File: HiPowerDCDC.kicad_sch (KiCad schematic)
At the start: 57 parts, among them J1 Conn_01x01, J2 Conn_01x01, J3 Conn_01x01, J4 Conn_01x01, J5 Conn_01x04, Q1 WMJ38N60, Q2 WMJ38N60, SW1 SW_Push, SW2 SW_Push, U1 ESP32-WROOM-32U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

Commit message: Changed to high voltage capacitors
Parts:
- C11, C12, C13, C14: footprint Capacitor_SMD:C_1206_3216Metric -> Capacitor_SMD:C_1812_4532Metric
- R10: footprint Resistor_SMD:R_1206_3216Metric -> Resistor_SMD:R_1812_4532Metric
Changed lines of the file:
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@@
       (effects (font (size 1.27 1.27)) (justify left))
     )
-    (property "Footprint" "Resistor_SMD:R_1206_3216Metric" (id 2) (at 184.277 137.795 90)
+    (property "Footprint" "Resistor_SMD:R_1812_4532Metric" (id 2) (at 184.277 137.795 90)
       (effects (font (size 1.27 1.27)) hide)
     )
@@
       (effects (font (size 1.27 1.27)) (justify left))
     )
-    (property "Footprint" "Capacitor_SMD:C_1206_3216Metric" (id 2) (at 204.1652 83.185 0)
+    (property "Footprint" "Capacitor_SMD:C_1812_4532Metric" (id 2) (at 204.1652 83.185 0)
       (effects (font (size 1.27 1.27)) hide)
     )
@@
       (effects (font (size 1.27 1.27)) (justify left))
     )
-    (property "Footprint" "Capacitor_SMD:C_1206_3216Metric" (id 2) (at 204.1652 139.7 0)
+    (property "Footprint" "Capacitor_SMD:C_1812_4532Metric" (id 2) (at 204.1652 139.7 0)
       (effects (font (size 1.27 1.27)) hide)
     )
@@
       (effects (font (size 1.27 1.27)) (justify left))
     )
-    (property "Footprint" "Capacitor_SMD:C_1206_3216Metric" (id 2) (at 209.8802 83.185 0)
+    (property "Footprint" "Capacitor_SMD:C_1812_4532Metric" (id 2) (at 209.8802 83.185 0)
       (effects (font (size 1.27 1.27)) hide)
     )
@@
       (effects (font (size 1.27 1.27)) (justify left))
     )
-    (property "Footprint" "Capacitor_SMD:C_1206_3216Metric" (id 2) (at 209.8802 139.7 0)
+    (property "Footprint" "Capacitor_SMD:C_1812_4532Metric" (id 2) (at 209.8802 139.7 0)
       (effects (font (size 1.27 1.27)) hide)
     )
@@
     )
     (path "/1d6ca196-d190-42cc-82e2-dd05479e359d"
-      (reference "C11") (unit 1) (value "10n") (footprint "Capacitor_SMD:C_1206_3216Metric")
+      (reference "C11") (unit 1) (value "10n") (footprint "Capacitor_SMD:C_1812_4532Metric")
     )
     (path "/40521bdb-9910-4911-97bc-1c460c9e71b9"
-      (reference "C12") (unit 1) (value "10n") (footprint "Capacitor_SMD:C_1206_3216Metric")
+      (reference "C12") (unit 1) (value "10n") (footprint "Capacitor_SMD:C_1812_4532Metric")
     )
     (path "/116f1552-f56f-4cf6-88c9-0aac35b221be"
-      (reference "C13") (unit 1) (value "10n") (footprint "Capacitor_SMD:C_1206_3216Metric")
+      (reference "C13") (unit 1) (value "10n") (footprint "Capacitor_SMD:C_1812_4532Metric")
     )
     (path "/e4d3f805-887c-499c-a2d1-0322c8808f2b"
-      (reference "C14") (unit 1) (value "10n") (footprint "Capacitor_SMD:C_1206_3216Metric")
+      (reference "C14") (unit 1) (value "10n") (footprint "Capacitor_SMD:C_1812_4532Metric")
     )
     (path "/212825e7-4ffe-4953-87c8-beb79db8e49b"
@@
     )
     (path "/f27ca728-3ec4-4b64-b597-7f763991f368"
-      (reference "R10") (unit 1) (value "10M") (footprint "Resistor_SMD:R_1206_3216Metric")
+      (reference "R10") (unit 1) (value "10M") (footprint "Resistor_SMD:R_1812_4532Metric")
     )
     (path "/31561b39-b331-494c-9b8f-ce3ac83f19cc"

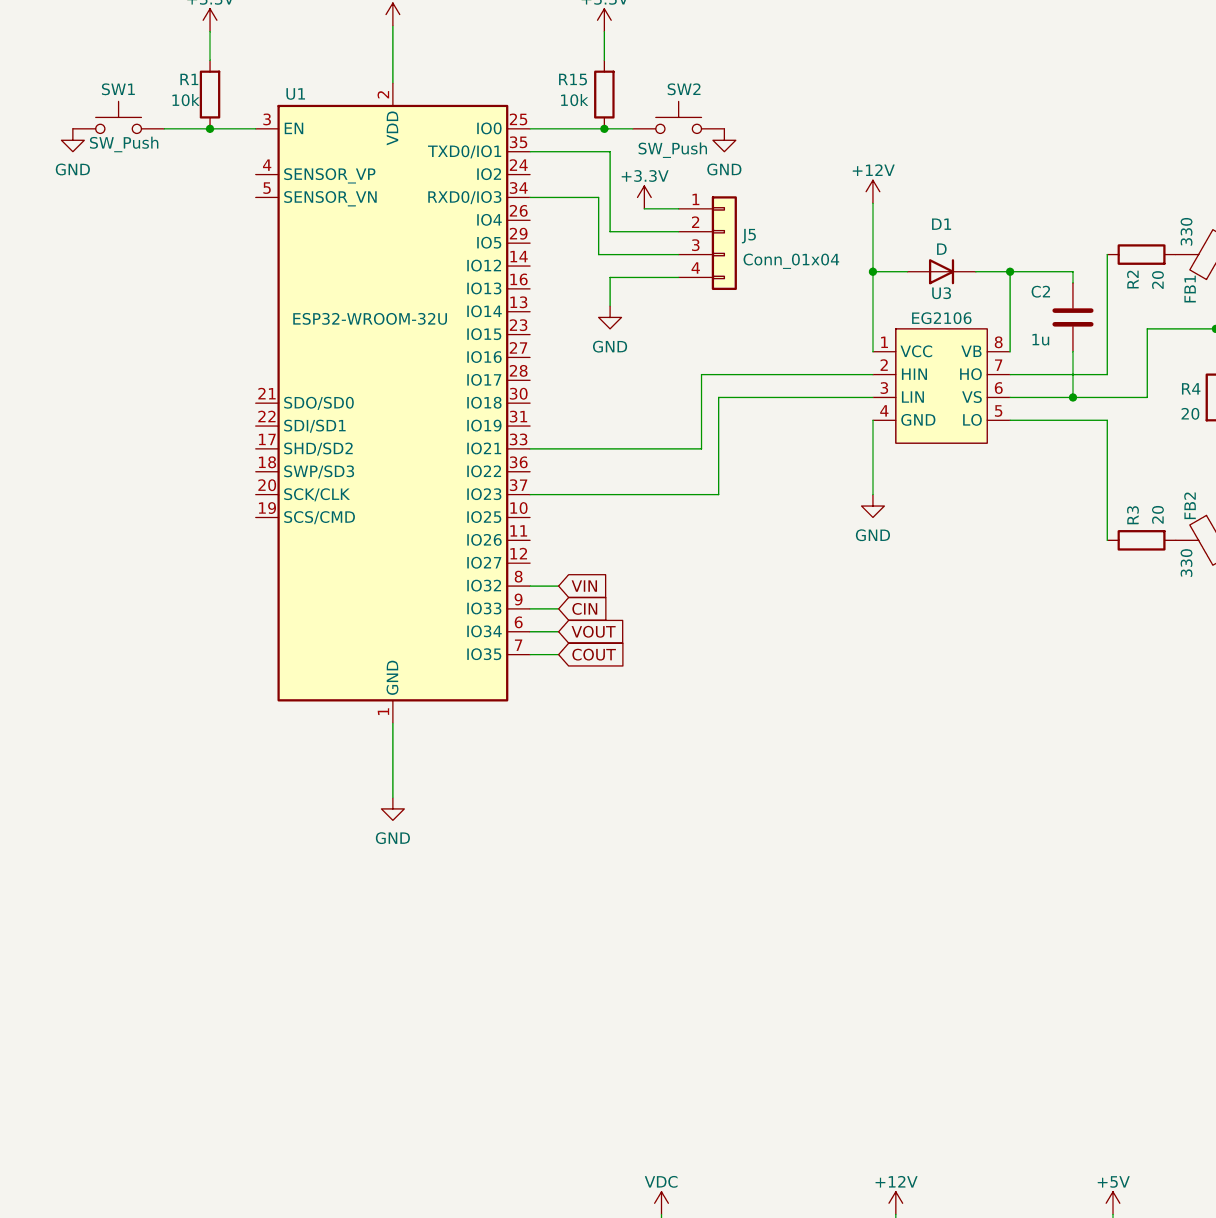
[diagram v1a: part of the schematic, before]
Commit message: Added PTC sensor, Laci you didn't check me :(
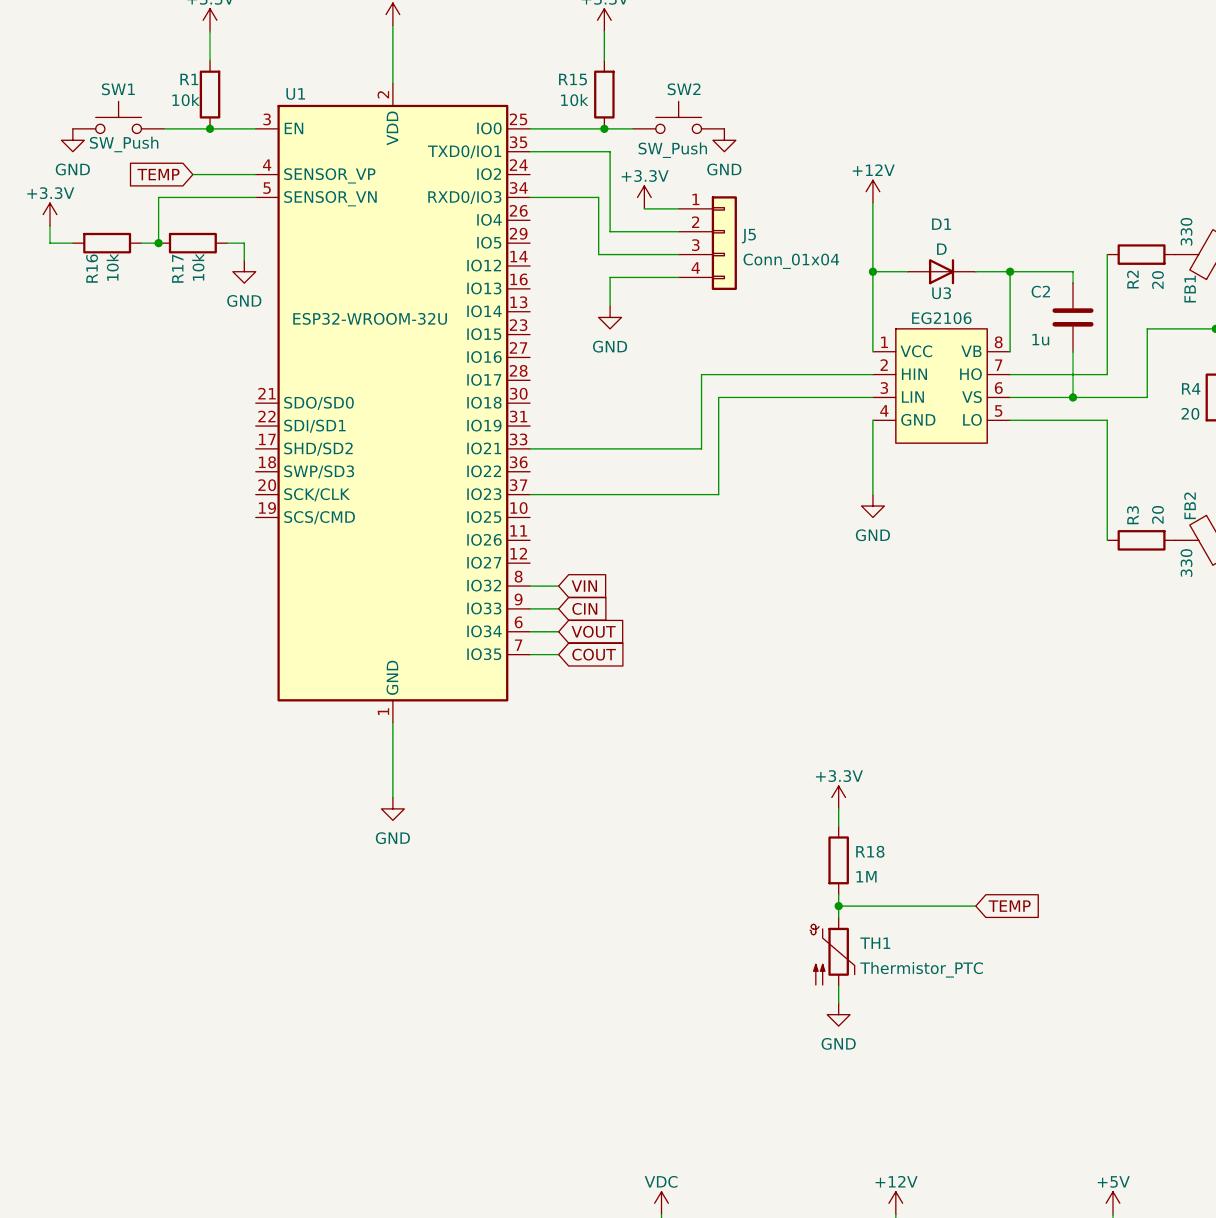
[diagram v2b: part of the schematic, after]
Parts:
- added R16, R17: 10k, Resistor_SMD:R_1206_3216Metric, symbol Device:R
- added R18: 1M, Resistor_SMD:R_1206_3216Metric, symbol Device:R
- added TH1: Thermistor_PTC, Connector_PinHeader_2.54mm:PinHeader_1x02_P2.54mm_Vertical, symbol Device:Thermistor_PTC
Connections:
- net +3V3: now also R16.2, R18.1
- net GND: now also R17.1, TH1.2
- net TEMP: now reaches U1.4 (SENSOR_VP)
- net TEMP: now also R18.2, TH1.1
- net at U1.5 (SENSOR_VN): now also R16.1, R17.2

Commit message: Added Keystone connectors
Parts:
- J1, J2, J3, J4: footprint HiPowerFP:Screw_PCB_pin -> HiPowerFP:Keystone_7808
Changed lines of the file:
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@@
       (effects (font (size 1.27 1.27)) (justify left))
     )
-    (property "Footprint" "HiPowerFP:Screw_PCB_pin" (id 2) (at 250.19 75.565 0)
-      (effects (font (size 1.27 1.27)) hide)
-    )
-    (property "Datasheet" "~" (id 3) (at 250.19 75.565 0)
+    (property "Footprint" "HiPowerFP:Keystone_7808" (id 2) (at 250.19 75.565 0)
+      (effects (font (size 1.27 1.27)) hide)
+    )
+    (property "Datasheet" "${KIPRJMOD}/datasheets/7808_keystone.pdf" (id 3) (at 250.19 75.565 0)
       (effects (font (size 1.27 1.27)) hide)
     )
@@
       (effects (font (size 1.27 1.27)) (justify left))
     )
-    (property "Footprint" "HiPowerFP:Screw_PCB_pin" (id 2) (at 250.19 84.455 0)
-      (effects (font (size 1.27 1.27)) hide)
-    )
-    (property "Datasheet" "~" (id 3) (at 250.19 84.455 0)
+    (property "Footprint" "HiPowerFP:Keystone_7808" (id 2) (at 250.19 84.455 0)
+      (effects (font (size 1.27 1.27)) hide)
+    )
+    (property "Datasheet" "${KIPRJMOD}/datasheets/7808_keystone.pdf" (id 3) (at 250.19 84.455 0)
       (effects (font (size 1.27 1.27)) hide)
     )
@@
       (effects (font (size 1.27 1.27)) (justify left))
     )
-    (property "Footprint" "HiPowerFP:Screw_PCB_pin" (id 2) (at 250.19 132.08 0)
-      (effects (font (size 1.27 1.27)) hide)
-    )
-    (property "Datasheet" "~" (id 3) (at 250.19 132.08 0)
+    (property "Footprint" "HiPowerFP:Keystone_7808" (id 2) (at 250.19 132.08 0)
+      (effects (font (size 1.27 1.27)) hide)
+    )
+    (property "Datasheet" "${KIPRJMOD}/datasheets/7808_keystone.pdf" (id 3) (at 250.19 132.08 0)
       (effects (font (size 1.27 1.27)) hide)
     )
@@
       (effects (font (size 1.27 1.27)) (justify left))
     )
-    (property "Footprint" "HiPowerFP:Screw_PCB_pin" (id 2) (at 250.19 140.97 0)
-      (effects (font (size 1.27 1.27)) hide)
-    )
-    (property "Datasheet" "~" (id 3) (at 250.19 140.97 0)
+    (property "Footprint" "HiPowerFP:Keystone_7808" (id 2) (at 250.19 140.97 0)
+      (effects (font (size 1.27 1.27)) hide)
+    )
+    (property "Datasheet" "${KIPRJMOD}/datasheets/7808_keystone.pdf" (id 3) (at 250.19 140.97 0)
       (effects (font (size 1.27 1.27)) hide)
     )
@@
     )
     (path "/56e6dc88-8c88-4439-9853-8d5650f4e59a"
-      (reference "J1") (unit 1) (value "Conn_01x01") (footprint "HiPowerFP:Screw_PCB_pin")
-    )
-    (path "/b86069d6-ba7b-4fda-bab9-b3b8645a27eb"
-      (reference "J2") (unit 1) (value "Conn_01x01") (footprint "HiPowerFP:Screw_PCB_pin")
-    )
-    (path "/a601ba08-1f80-4e43-833f-dc284503f818"
-      (reference "J3") (unit 1) (value "Conn_01x01") (footprint "HiPowerFP:Screw_PCB_pin")
-    )
-    (path "/9db3a826-765e-4e20-9c06-c40423065459"
-      (reference "J4") (unit 1) (value "Conn_01x01") (footprint "HiPowerFP:Screw_PCB_pin")
+      (reference "J1") (unit 1) (value "Conn_01x01") (footprint "HiPowerFP:Keystone_7808")
+    )
+    (path "/06783550-9719-4bf5-8140-cd255df7e49f"
+      (reference "J2") (unit 1) (value "Conn_01x01") (footprint "HiPowerFP:Keystone_7808")
+    )
+    (path "/67875fcf-d422-48b1-a954-a524082b2bfd"
+      (reference "J3") (unit 1) (value "Conn_01x01") (footprint "HiPowerFP:Keystone_7808")
+    )
+    (path "/b9d475bc-116f-4967-8e26-e7975b071a1b"
+      (reference "J4") (unit 1) (value "Conn_01x01") (footprint "HiPowerFP:Keystone_7808")
     )
     (path "/b7572976-7ea1-460a-b8f3-b2f7dbe7301b"

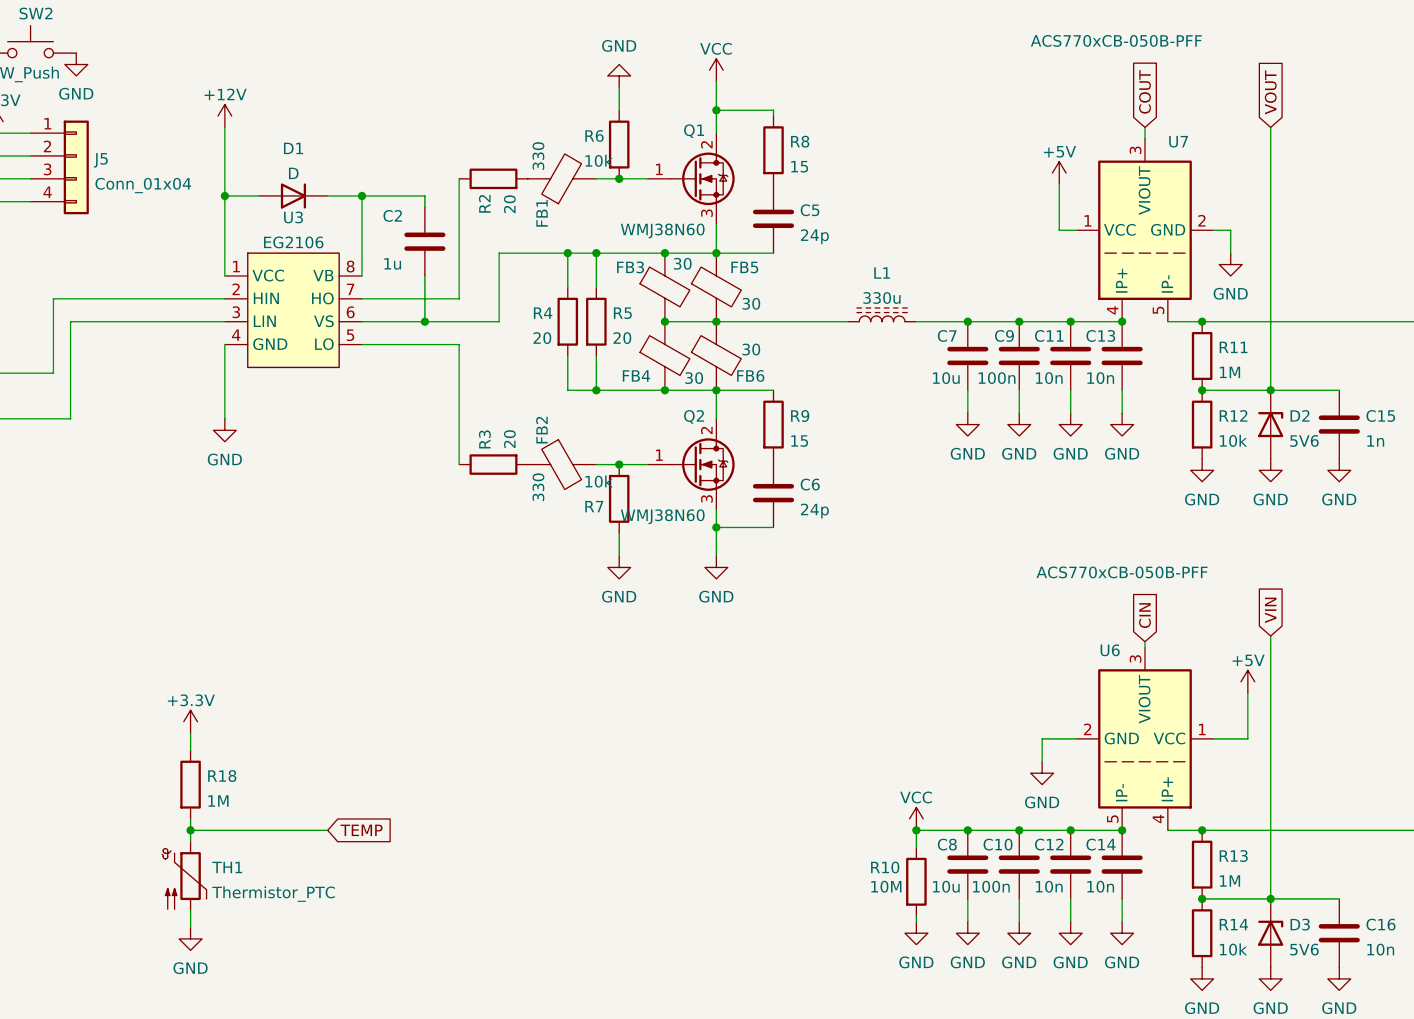
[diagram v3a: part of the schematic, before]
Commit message: Changed FR107 footprint
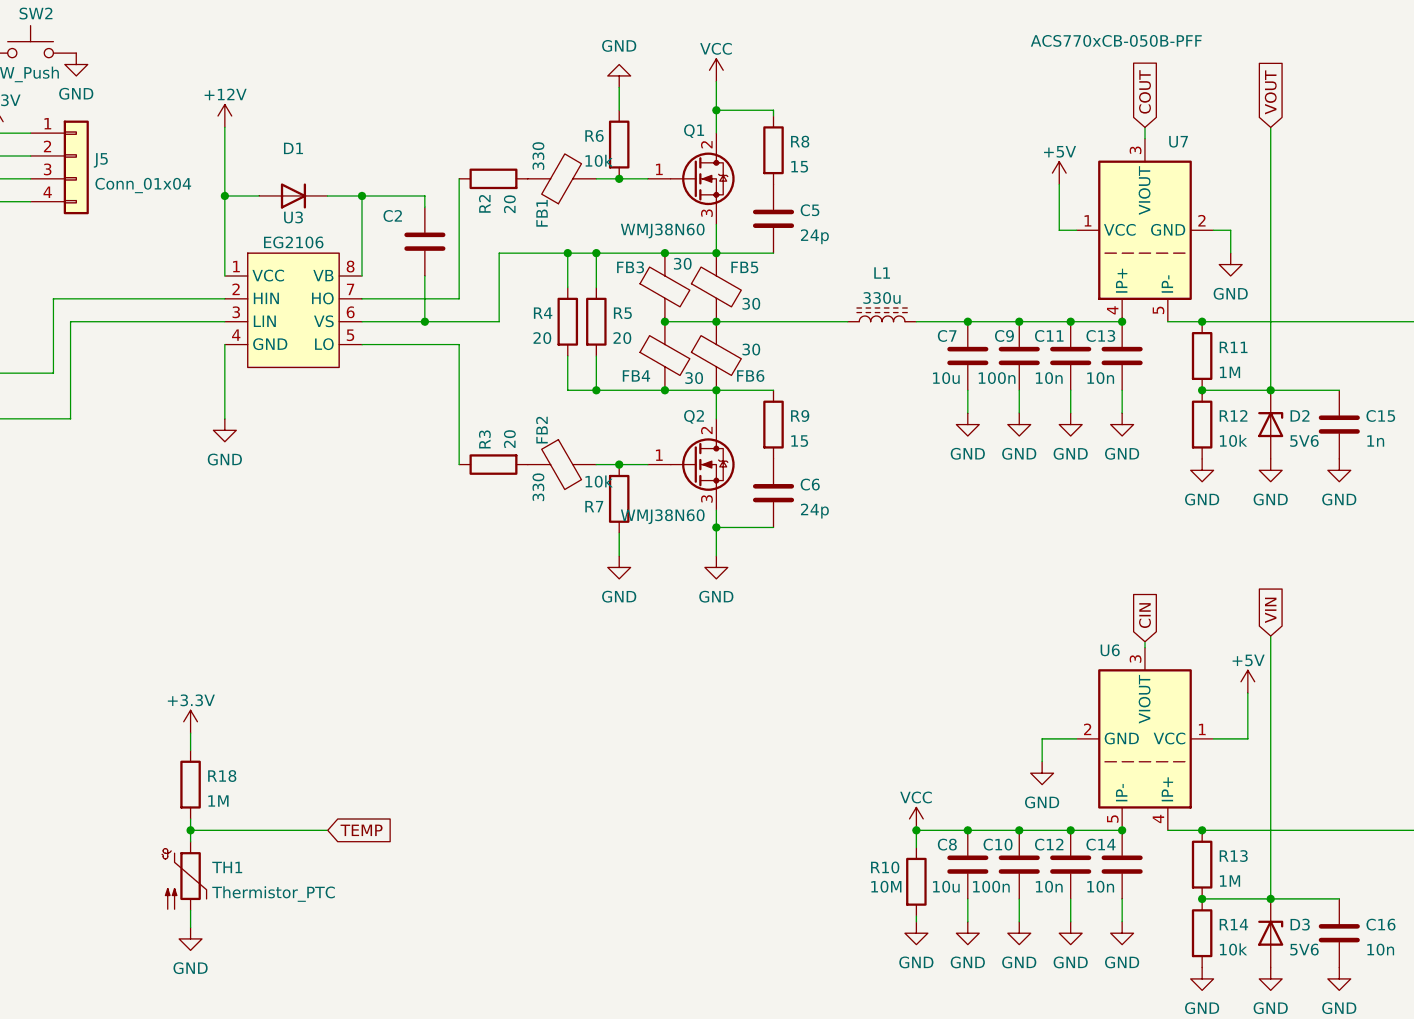
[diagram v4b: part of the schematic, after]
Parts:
- C2: value 1u -> (none); footprint Capacitor_SMD:C_1206_3216Metric -> (none)
- D1: value D -> (none); footprint Diode_SMD:D_1206_3216Metric -> (none); Distributor (none) -> www.lcsc.com
- U6: value ACS770xCB-050B-PFF -> (none); footprint Sensor_Current:Allegro_CB_PFF -> (none)

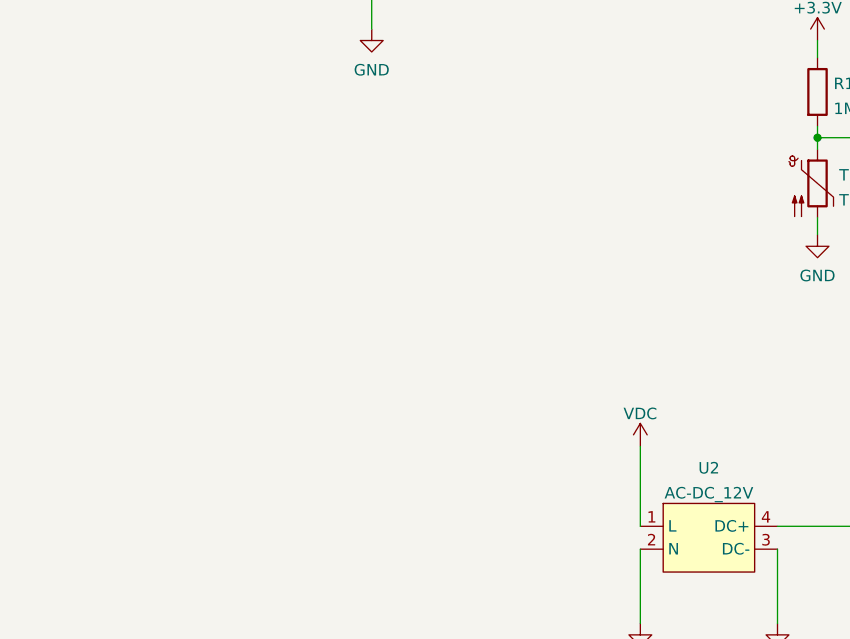
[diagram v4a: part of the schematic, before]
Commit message: Increased PCB width and made high P component more spaceous
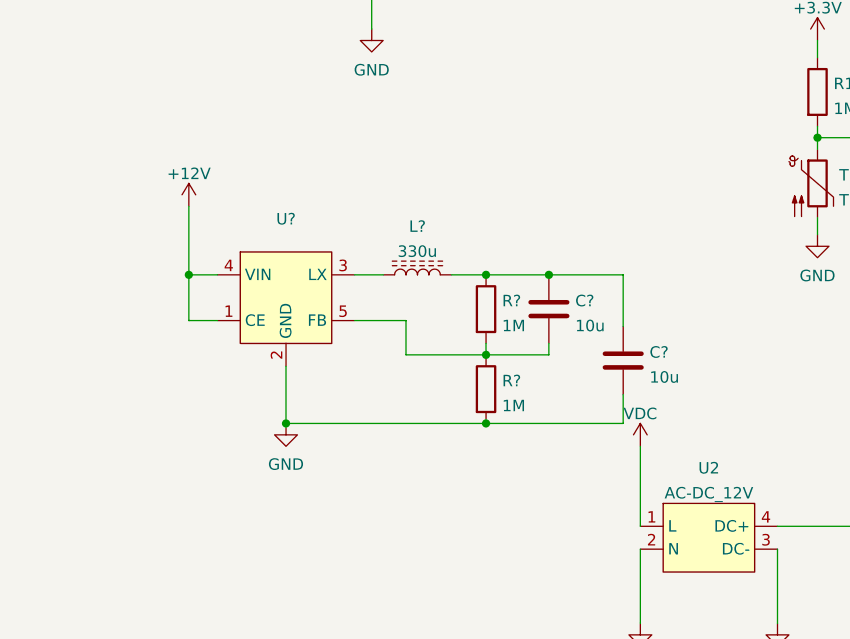
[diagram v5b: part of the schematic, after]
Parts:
- added C? (x2): 10u, Capacitor_SMD:C_1206_3216Metric, symbol Device:C
- added L?: 330u, Inductor_THT:L_Toroid_Vertical_L54.0mm_W23.8mm_P20.10mm_Bourns_5700, symbol Device:L_Ferrite
- added R? (x2): 1M, Resistor_SMD:R_1206_3216Metric, symbol Device:R
- added U?: (no value), Package_TO_SOT_SMD:SOT-23-5, symbol SolarLibrary:XT3410
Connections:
- net +12V: now also U?.1 (CE), U?.4 (VIN)
- net GND: now also C?.2, R?.2, U?.2 (GND)
- new net: C?.1, C?.1, L?.2, R?.1
- new net: C?.2, R?.1, R?.2, U?.5 (FB)
- new net: L?.1, U?.3 (LX)
